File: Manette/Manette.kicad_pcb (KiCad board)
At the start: 2 copper layers, 120 x 80 mm, 19 parts, among them J2 Barrel_Jack, SW1 SW_SPST, SW2 SW_Push, SW3 SW_Push, SW4 SW_Push, SW5 SW_Push, SW6 SW_Push, U1 LD1117S33TR_SOT223, U2 ESP32-S3-WROOM-1

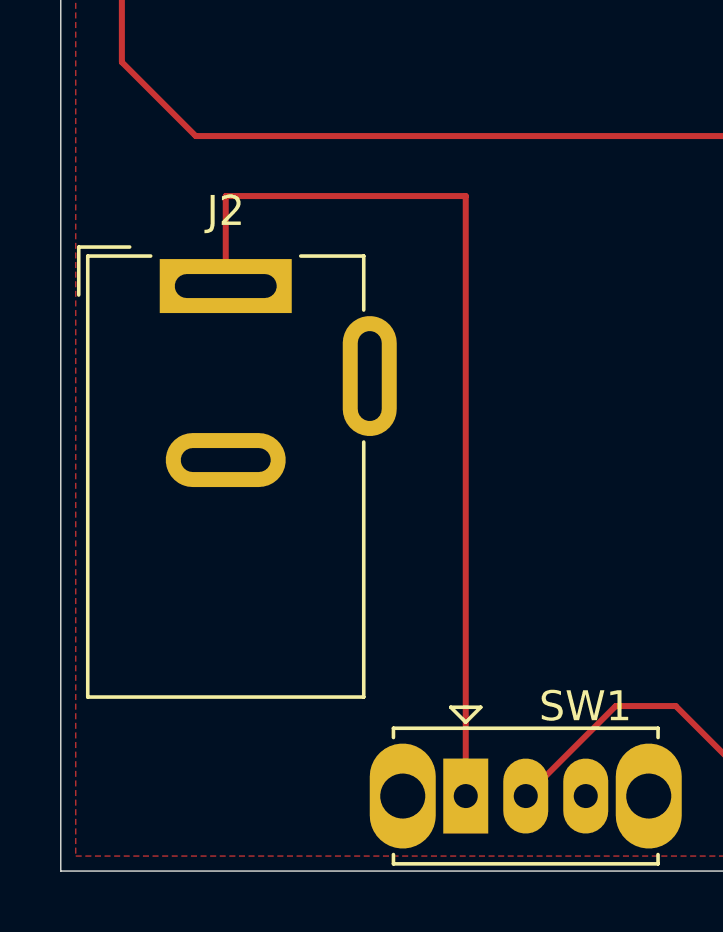
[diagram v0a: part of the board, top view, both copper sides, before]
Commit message: fix(manette): removed the barrel jack with a 2 pin connector to place the 4 battery holder
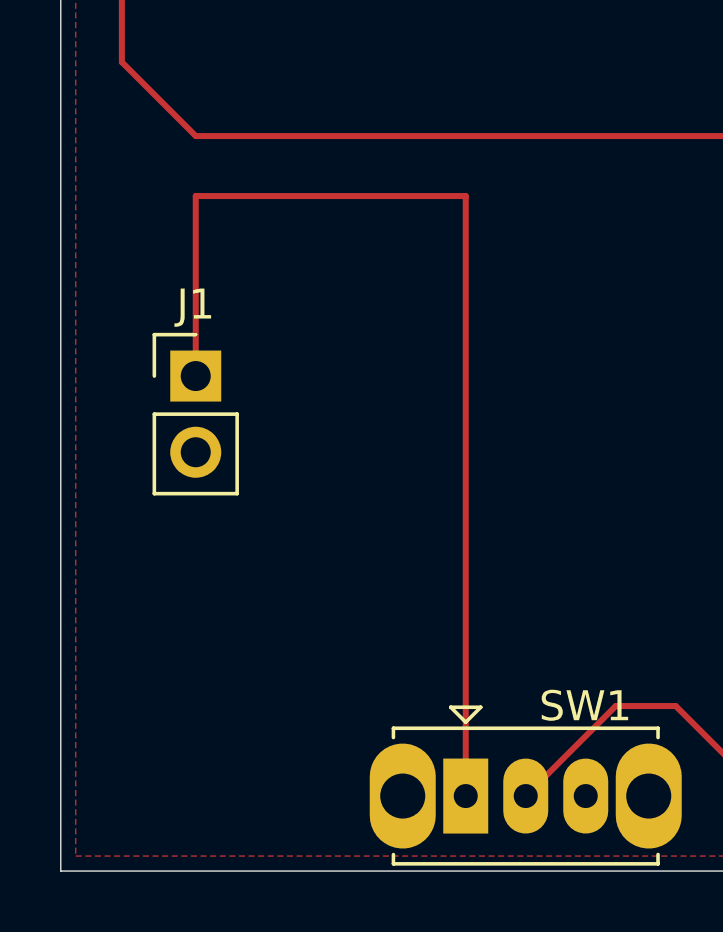
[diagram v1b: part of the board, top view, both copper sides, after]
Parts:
- removed J2: Barrel_Jack, Connector_BarrelJack:BarrelJack_Wuerth_6941xx301002
- added J1: Conn_01x02_Pin, Connector_PinHeader_2.54mm:PinHeader_1x02_P2.54mm_Vertical, F.Cu at (85.0, 119.0)
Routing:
- net Net-(J1-Pin_1): track 31.0 -> 35.0 mm
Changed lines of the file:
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@@
 	(net 4 "Net-(D1-DIN)")
 	(net 5 "unconnected-(D1-DOUT-Pad2)")
-	(net 6 "Net-(SW1-A)")
+	(net 6 "Net-(J1-Pin_1)")
 	(net 7 "Net-(U2-EN)")
 	(net 8 "/IO4")
@@
 			(layers "*.Cu" "*.Mask")
 			(remove_unused_layers no)
-			(net 6 "Net-(SW1-A)")
+			(net 6 "Net-(J1-Pin_1)")
 			(pinfunction "A")
 			(pintype "passive")
@@
 		)
 	)
-	(footprint "Connector_BarrelJack:BarrelJack_Wuerth_6941xx301002"
+	(footprint "Connector_PinHeader_2.54mm:PinHeader_1x02_P2.54mm_Vertical"
 		(layer "F.Cu")
-		(at 86 116)
-		(descr "Wuerth electronics barrel jack connector (5.5mm outher diameter, inner diameter 2.05mm or 2.55mm depending on exact order number), See: http://katalog.we-online.de/em/datasheet/6941xx301002.pdf")
-		(tags "connector barrel jack")
-		(property "Reference" "J2"
-			(at 0 -2.5 0)
+		(at 85 119)
+		(descr "Through hole straight pin header, 1x02, 2.54mm pitch, single row")
+		(tags "Through hole pin header THT 1x02 2.54mm single row")
+		(property "Reference" "J1"
+			(at 0 -2.38 0)
 			(layer "F.SilkS")
 			(effects
@@
 			)
 		)
-		(property "Value" "Barrel_Jack"
-			(at 0 15.5 0)
+		(property "Value" "Conn_01x02_Pin"
+			(at 0 4.92 0)
 			(layer "F.Fab")
 			(effects
@@
 		(property "Datasheet" ""
 			(at 0 0 0)
-			(unlocked yes)
 			(layer "F.Fab")
 			(hide yes)
@@
 			)
 		)
-		(property "Description" "DC Barrel Jack"
+		(property "Description" "Generic connector, single row, 01x02, script generated"
 			(at 0 0 0)
-			(unlocked yes)
 			(layer "F.Fab")
 			(hide yes)
@@
 			)
 		)
-		(property ki_fp_filters "BarrelJack*")
+		(property ki_fp_filters "Connector*:*_1x??_*")
 		(sheetname "/")
 		(sheetfile "Manette.kicad_sch")
 		(attr through_hole)
 		(fp_line
-			(start -4.9 -1.3)
-			(end -4.9 0.3)
-			(stroke
-				(width 0.12)
-				(type solid)
-			)
-			(layer "F.SilkS")
-		)
-		(fp_line
-			(start -4.6 -1)
-			(end -2.5 -1)
+			(start -1.38 -1.38)
+			(end 0 -1.38)
 			(stroke
 				(width 0.12)
@@
 		)
 		(fp_line
-			(start -4.6 13.7)
-			(end -4.6 -1)
+			(start -1.38 0)
+			(end -1.38 -1.38)
 			(stroke
 				(width 0.12)
@@
 		)
 		(fp_line
-			(start -3.2 -1.3)
-			(end -4.9 -1.3)
+			(start -1.38 1.27)
+			(end -1.38 3.92)
 			(stroke
 				(width 0.12)
@@
 		)
 		(fp_line
-			(start 2.5 -1)
-			(end 4.6 -1)
+			(start -1.38 1.27)
+			(end 1.38 1.27)
 			(stroke
 				(width 0.12)
@@
 		)
 		(fp_line
-			(start 4.6 -1)
-			(end 4.6 0.8)
+			(start -1.38 3.92)
+			(end 1.38 3.92)
 			(stroke
 				(width 0.12)
@@
 		)
 		(fp_line
-			(start 4.6 5.2)
-			(end 4.6 13.7)
+			(start 1.38 1.27)
+			(end 1.38 3.92)
 			(stroke
 				(width 0.12)
@@
 		)
 		(fp_line
-			(start 4.6 13.7)
-			(end -4.6 13.7)
-			(stroke
-				(width 0.12)
-				(type solid)
-			)
-			(layer "F.SilkS")
-		)
-		(fp_line
-			(start -5 -1.4)
-			(end -5 14.1)
-			(stroke
-				(width 0.05)
-				(type solid)
-			)
-			(layer "F.CrtYd")
-		)
-		(fp_line
-			(start -5 14.1)
-			(end 5 14.1)
-			(stroke
-				(width 0.05)
-				(type solid)
-			)
-			(layer "F.CrtYd")
-		)
-		(fp_line
-			(start 5 -1.4)
-			(end -5 -1.4)
-			(stroke
-				(width 0.05)
-				(type solid)
-			)
-			(layer "F.CrtYd")
-		)
-		(fp_line
-			(start 5 0.5)
-			(end 5 -1.4)
+			(start -1.77 -1.77)
+			(end -1.77 4.32)
 			(stroke
 				(width 0.05)
@@
 		)
 		(fp_line
-			(start 5 14.1)
-			(end 5 5.5)
+			(start -1.77 4.32)
+			(end 1.77 4.32)
 			(stroke
 				(width 0.05)
@@
 		)
 		(fp_line
-			(start 6.2 0.5)
-			(end 5 0.5)
+			(start 1.77 -1.77)
+			(end -1.77 -1.77)
 			(stroke
 				(width 0.05)
@@
 		)
 		(fp_line
-			(start 6.2 0.5)
-			(end 6.2 5.5)
+			(start 1.77 4.32)
+			(end 1.77 -1.77)
 			(stroke
 				(width 0.05)
@@
 		)
 		(fp_line
-			(start 6.2 5.5)
-			(end 5 5.5)
-			(stroke
-				(width 0.05)
-				(type solid)
-			)
-			(layer "F.CrtYd")
-		)
-		(fp_line
-			(start -4.5 0.1)
-			(end -3.5 -0.9)
+			(start -1.27 -0.635)
+			(end -0.635 -1.27)
 			(stroke
 				(width 0.1)
@@
 		)
 		(fp_line
-			(start -4.5 13.6)
-			(end -4.5 0.1)
+			(start -1.27 3.81)
+			(end -1.27 -0.635)
 			(stroke
 				(width 0.1)
@@
 		)
 		(fp_line
-			(start 4.5 -0.9)
-			(end -3.5 -0.9)
+			(start -0.635 -1.27)
+			(end 1.27 -1.27)
 			(stroke
 				(width 0.1)
@@
 		)
 		(fp_line
-			(start 4.5 -0.9)
-			(end 4.5 13.6)
+			(start 1.27 -1.27)
+			(end 1.27 3.81)
 			(stroke
 				(width 0.1)
@@
 		)
 		(fp_line
-			(start 4.5 13.6)
-			(end -4.5 13.6)
+			(start 1.27 3.81)
+			(end -1.27 3.81)
 			(stroke
 				(width 0.1)
@@
 		)
 		(fp_text user "${REFERENCE}"
-			(at 0 7.5 0)
+			(at 0 1.27 90)
 			(layer "F.Fab")
 			(effects
@@
 		(pad "1" thru_hole rect
 			(at 0 0)
-			(size 4.4 1.8)
-			(drill oval 3.4 0.8)
+			(size 1.7 1.7)
+			(drill 1)
 			(layers "*.Cu" "*.Mask")
 			(remove_unused_layers no)
-			(net 6 "Net-(SW1-A)")
+			(net 6 "Net-(J1-Pin_1)")
+			(pinfunction "Pin_1")
 			(pintype "passive")
 		)
-		(pad "2" thru_hole oval
-			(at 0 5.8)
-			(size 4 1.8)
-			(drill oval 3 0.8)
+		(pad "2" thru_hole circle
+			(at 0 2.54)
+			(size 1.7 1.7)
+			(drill 1)
 			(layers "*.Cu" "*.Mask")
 			(remove_unused_layers no)
 			(net 1 "GND")
+			(pinfunction "Pin_2")
 			(pintype "passive")
 		)
-		(pad "3" thru_hole oval
-			(at 4.8 3 90)
-			(size 4 1.8)
-			(drill oval 3 0.8)
-			(layers "*.Cu" "*.Mask")
-			(remove_unused_layers no)
-		)
 		(embedded_fonts no)
-		(model "${KICAD9_3DMODEL_DIR}/Connector_BarrelJack.3dshapes/BarrelJack_Wuerth_6941xx301002.step"
+		(model "${KICAD9_3DMODEL_DIR}/Connector_PinHeader_2.54mm.3dshapes/PinHeader_1x02_P2.54mm_Vertical.step"
 			(offset
 				(xyz 0 0 0)
@@
 	)
 	(segment
-		(start 86 113)
-		(end 94 113)
+		(start 94 113)
+		(end 85 113)
 		(width 0.2)
 		(layer "F.Cu")
@@
 	)
 	(segment
-		(start 94 113)
-		(end 94 133)
+		(start 94 133)
+		(end 94 113)
 		(width 0.2)
 		(layer "F.Cu")
@@
 	)
 	(segment
-		(start 86 116)
-		(end 86 113)
+		(start 85 113)
+		(end 85 119)
 		(width 0.2)
 		(layer "F.Cu")
